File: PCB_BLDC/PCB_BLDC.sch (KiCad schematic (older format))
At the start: 61 parts, among them J10 Conn_01x06, J11 Conn_01x07, J12 Conn_01x06, J13 Conn_01x08, J16 Conn_01x08, J17 Conn_01x10, J8 VCC_Unregulated, J9 VCC_GND, Q1 IRF4905, SW1 Rotary_Encoder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

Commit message: Main: Finish PCB Routing Add Filled Zone Texts
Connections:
- net 5V is gone; now on net VCC_5V: A1.5 (+5V), J13.5 (Pin_5)
- net L1_Sense: now also J11.4 (Pin_4); no longer J11.3 (Pin_3)
- net L2_Sense: now also J11.3 (Pin_3); no longer J11.2 (Pin_2)
- net L3_Sense: now also J11.2 (Pin_2); no longer J11.1 (Pin_1)
- net VCC_5V: now also J11.1 (Pin_1); no longer A1.8 (VIN), J11.4 (Pin_4), J13.8 (Pin_8)
- new net VIN: A1.8 (VIN), J13.8 (Pin_8)
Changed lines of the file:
@@
 Wire Wire Line
 	4600 1150 4550 1150
-Text Label 3300 3500 0    50   ~ 0
+Text Label 3100 3500 2    50   ~ 0
 VCC_5V
 Wire Wire Line
@@
 VCC_Filtered
 Text Label 3100 2300 2    50   ~ 0
-VCC_Filtered
-Text Label 5950 1150 0    50   ~ 0
 VCC_Filtered
 Text Notes 1250 650  0    50   ~ 0
@@
 Wire Notes Line
 	3400 850  6450 850
-Wire Wire Line
-	3100 3450 3100 3500
 $Comp
 L power:GND #PWR01
@@
 Wire Wire Line
 	4700 1900 4700 2000
-Text Label 5500 5000 2    50   ~ 0
-VCC_5V
 Text Label 4900 6950 2    50   ~ 0
 Rot_A_Pull_Up
@@
 Wire Wire Line
 	850  1150 1400 1150
-Wire Wire Line
-	3300 3500 3100 3500
-Connection ~ 3100 3500
-Wire Wire Line
-	3100 3500 3100 3650
 Text Label 750  5450 2    50   ~ 0
 Reset
@@
 Wire Wire Line
 	1000 5550 750  5550
-Text Label 750  5650 2    50   ~ 0
-5V
 Wire Wire Line
 	750  5650 1000 5650
@@
 Text Label 6300 6050 0    50   ~ 0
 AREF
-Text Label 750  5950 2    50   ~ 0
+Text Label 750  5650 2    50   ~ 0
 VCC_5V
 Text Label 5700 5000 2    50   ~ 0
@@
 Wire Wire Line
 	5500 5000 5500 5250
-Text Label 5800 5000 0    50   ~ 0
-5V
 Text Label 5700 7450 0    50   ~ 0
 GND
@@
 Wire Wire Line
 	6300 6250 6100 6250
-Wire Wire Line
-	3100 2700 3100 2800
+$Comp
+L Connector_Generic:Conn_01x06 J10
+U 1 1 61CCE6B7
+P 750 7250
+F 0 "J10" H 830 7242 50  0000 L CNN
+F 1 "Conn_01x06" H 830 7151 50  0000 L CNN
+F 2 "Connector_PinSocket_2.54mm:PinSocket_1x06_P2.54mm_Vertical" H 750 7250 50  0001 C CNN
+F 3 "~" H 750 7250 50  0001 C CNN
+	1    750  7250
+	-1   0    0    -1
+$EndComp
+Wire Wire Line
+	1050 7550 950  7550
+Wire Wire Line
+	950  7450 1050 7450
+Wire Wire Line
+	950  7350 1050 7350
+Text Label 1050 7350 0    50   ~ 0
+L1_Sense
+Text Label 1050 7450 0    50   ~ 0
+L2_Sense
+Text Label 1050 7550 0    50   ~ 0
+L3_Sense
+$Comp
+L Connector_Generic:Conn_01x07 J11
+U 1 1 61E26882
+P 3200 7300
+F 0 "J11" H 3118 6775 50  0000 C CNN
+F 1 "Conn_01x07" H 3118 6866 50  0000 C CNN
+F 2 "TerminalBlock_Phoenix:TerminalBlock_Phoenix_MKDS-1,5-7_1x07_P5.00mm_Horizontal" H 3200 7300 50  0001 C CNN
+F 3 "~" H 3200 7300 50  0001 C CNN
+	1    3200 7300
+	-1   0    0    1
+$EndComp
+Text Label 3550 7500 0    50   ~ 0
+L3_Sense
+Text Label 3550 7400 0    50   ~ 0
+L2_Sense
+Text Label 3550 7300 0    50   ~ 0
+L1_Sense
+Text Label 3550 7200 0    50   ~ 0
+L3_Motor
+Text Label 3550 7100 0    50   ~ 0
+L2_Motor
+Text Label 3550 7600 0    50   ~ 0
+VCC_5V
+Wire Wire Line
+	3550 7000 3400 7000
+Wire Wire Line
+	3550 7100 3400 7100
+Wire Wire Line
+	3400 7200 3550 7200
+Wire Wire Line
+	3550 7300 3400 7300
+Wire Wire Line
+	3400 7400 3550 7400
+Wire Wire Line
+	3400 7600 3550 7600
+Wire Wire Line
+	3400 7500 3550 7500
+Text Label 3550 7000 0    50   ~ 0
+L1_Motor
+Text Label 5800 5000 0    50   ~ 0
+VCC_5V
+Text Label 5500 5000 2    50   ~ 0
+VIN
+Text Label 750  5950 2    50   ~ 0
+VIN
 $Comp
 L power:PWR_FLAG #FLG0103
 U 1 1 61C961E6
-P 5800 1150
-F 0 "#FLG0103" H 5800 1225 50  0001 C CNN
-F 1 "PWR_FLAG" H 5800 1323 50  0000 C CNN
-F 2 "" H 5800 1150 50  0001 C CNN
-F 3 "~" H 5800 1150 50  0001 C CNN
-	1    5800 1150
-	1    0    0    -1
-$EndComp
+P 5950 1150
+F 0 "#FLG0103" H 5950 1225 50  0001 C CNN
+F 1 "PWR_FLAG" H 5950 1323 50  0000 C CNN
+F 2 "" H 5950 1150 50  0001 C CNN
+F 3 "~" H 5950 1150 50  0001 C CNN
+	1    5950 1150
+	1    0    0    -1
+$EndComp
+Wire Wire Line
+	3100 2800 3100 2850
+Wire Wire Line
+	3100 2700 3100 2800
+Connection ~ 3100 2800
 $Comp
 L power:PWR_FLAG #FLG0104
@@
 	0    -1   -1   0
 $EndComp
-Connection ~ 3100 2800
-Wire Wire Line
-	3100 2800 3100 2850
-$Comp
-L Connector_Generic:Conn_01x06 J10
-U 1 1 61CCE6B7
-P 750 7250
-F 0 "J10" H 830 7242 50  0000 L CNN
-F 1 "Conn_01x06" H 830 7151 50  0000 L CNN
-F 2 "Connector_PinSocket_2.54mm:PinSocket_1x06_P2.54mm_Vertical" H 750 7250 50  0001 C CNN
-F 3 "~" H 750 7250 50  0001 C CNN
-	1    750  7250
-	-1   0    0    -1
-$EndComp
-Wire Wire Line
-	1050 7550 950  7550
-Wire Wire Line
-	950  7450 1050 7450
-Wire Wire Line
-	950  7350 1050 7350
-Text Label 1050 7350 0    50   ~ 0
-L1_Sense
-Text Label 1050 7450 0    50   ~ 0
-L2_Sense
-Text Label 1050 7550 0    50   ~ 0
-L3_Sense
-$Comp
-L Connector_Generic:Conn_01x07 J11
-U 1 1 61E26882
-P 3200 7300
-F 0 "J11" H 3118 6775 50  0000 C CNN
-F 1 "Conn_01x07" H 3118 6866 50  0000 C CNN
-F 2 "TerminalBlock_Phoenix:TerminalBlock_Phoenix_MKDS-1,5-7_1x07_P5.00mm_Horizontal" H 3200 7300 50  0001 C CNN
-F 3 "~" H 3200 7300 50  0001 C CNN
-	1    3200 7300
-	-1   0    0    1
-$EndComp
-Text Label 3550 7600 0    50   ~ 0
-L3_Sense
-Text Label 3550 7500 0    50   ~ 0
-L2_Sense
-Text Label 3550 7400 0    50   ~ 0
-L1_Sense
-Text Label 3550 7200 0    50   ~ 0
-L3_Motor
-Text Label 3550 7100 0    50   ~ 0
-L2_Motor
-Text Label 3550 7300 0    50   ~ 0
-VCC_5V
-Wire Wire Line
-	3550 7000 3400 7000
-Wire Wire Line
-	3550 7100 3400 7100
-Wire Wire Line
-	3400 7200 3550 7200
-Wire Wire Line
-	3550 7300 3400 7300
-Wire Wire Line
-	3400 7400 3550 7400
-Wire Wire Line
-	3400 7600 3550 7600
-Wire Wire Line
-	3400 7500 3550 7500
-Text Label 3550 7000 0    50   ~ 0
-L1_Motor
+Wire Wire Line
+	3100 3450 3100 3650
+Text Label 5550 1150 1    50   ~ 0
+VCC_Filtered
 $EndSCHEMATC

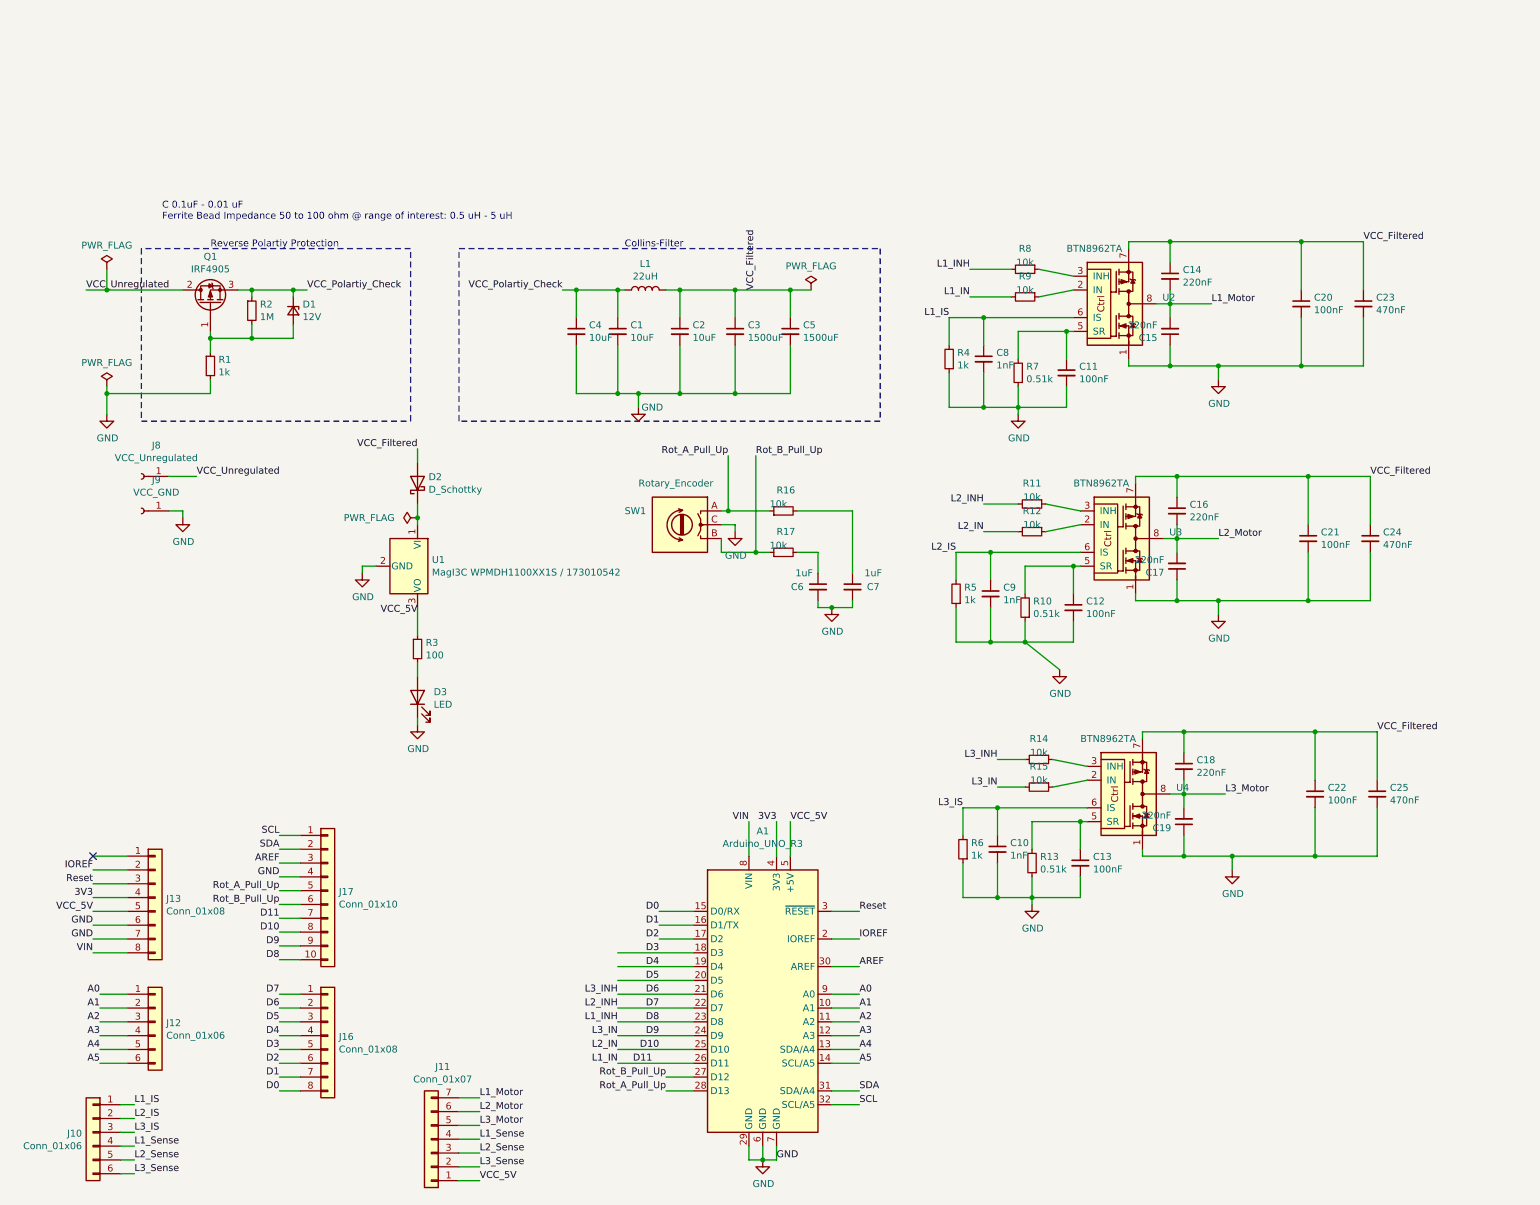
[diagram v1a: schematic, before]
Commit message: Main: Add Text to Schematic and PCB, Images
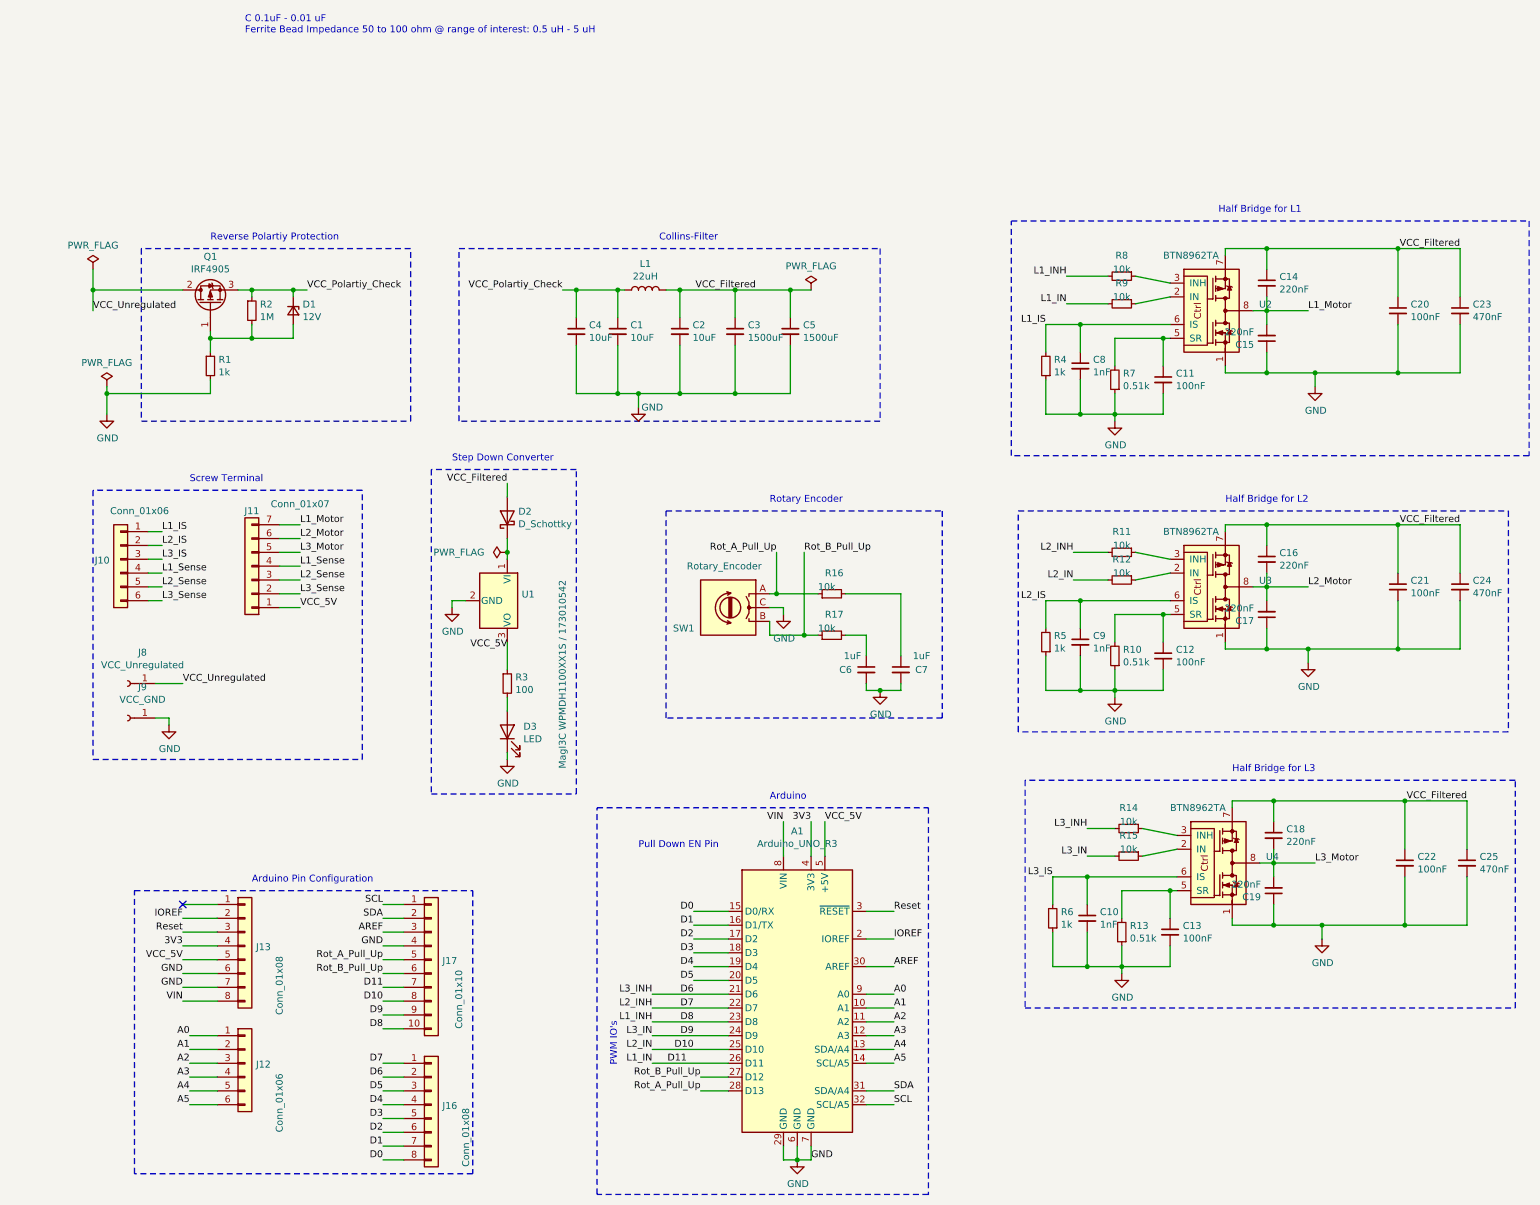
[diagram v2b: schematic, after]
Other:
- note added: "Arduino Pin Configuration\n"
- note added: "Arduino\n"
- note added: "Half Bridge for L1"
- note added: "Half Bridge for L2\n"
- note added: "Half Bridge for L3\n"
- note added: "PWM IO's"
- note added: "Pull Down EN Pin\n"
- note added: "Rotary Encoder"
- note added: "Screw Terminal"
- note added: "Step Down Converter\n"
- moved on the sheet: A1, C10, C11, C12, C13, C14, C15, C16, C17, C18, C19, C20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

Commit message: Main: Update PCB, Add Vias, Update Schematic, Update Netlist
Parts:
- removed J11: Conn_01x07, TerminalBlock_Phoenix:TerminalBlock_Phoenix_MKDS-1,5-7_1x07_P5.00mm_Horizontal, symbol Connector_Generic:Conn_01x07
- removed J9: VCC_GND, Connector:Banana_Jack_1Pin, symbol Connector:Conn_01x01_Female
- added J1: Conn_01x08, TerminalBlock_Phoenix:TerminalBlock_Phoenix_MKDS-1,5-8_1x08_P5.00mm_Horizontal, symbol Connector_Generic:Conn_01x08
- C1, C2, C4: footprint Capacitor_SMD:C_1206_3216Metric_Pad1.33x1.80mm_HandSolder -> Capacitor_SMD:C_1210_3225Metric_Pad1.33x2.70mm_HandSolder
- J8: value VCC_Unregulated -> Power Terminal; footprint Connector:Banana_Jack_1Pin -> Connector:Banana_Jack_2Pin; symbol Connector:Conn_01x01_Female -> Connector:Conn_01x02_Female
- R3: value 100 -> 150
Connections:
- net GND: now also J8.2 (Pin_2), J1.1 (Pin_1)
- net L1_Motor: now also J1.8 (Pin_8)
- net L1_Sense: now also J1.5 (Pin_5)
- net L2_Motor: now also J1.7 (Pin_7)
- net L2_Sense: now also J1.4 (Pin_4)
- net L3_Motor: now also J1.6 (Pin_6)
- net L3_Sense: now also J1.3 (Pin_3)
- net VCC_5V: now also J1.2 (Pin_2)
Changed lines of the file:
@@
 F 0 "C1" H 4642 1496 50  0000 L CNN
 F 1 "10uF" H 4642 1405 50  0000 L CNN
-F 2 "Capacitor_SMD:C_1206_3216Metric_Pad1.33x1.80mm_HandSolder" H 4550 1450 50  0001 C CNN
+F 2 "Capacitor_SMD:C_1210_3225Metric_Pad1.33x2.70mm_HandSolder" H 4550 1450 50  0001 C CNN
 F 3 "~" H 4550 1450 50  0001 C CNN
 	1    4550 1450
@@
 P 3750 4000
 F 0 "R3" H 3809 4046 50  0000 L CNN
-F 1 "100" H 3809 3955 50  0000 L CNN
+F 1 "150" H 3809 3955 50  0000 L CNN
 F 2 "Resistor_SMD:R_1206_3216Metric_Pad1.30x1.75mm_HandSolder" H 3750 4000 50  0001 C CNN
 F 3 "~" H 3750 4000 50  0001 C CNN
@@
 F 0 "C2" H 5092 1496 50  0000 L CNN
 F 1 "10uF" H 5092 1405 50  0000 L CNN
-F 2 "Capacitor_SMD:C_1206_3216Metric_Pad1.33x1.80mm_HandSolder" H 5000 1450 50  0001 C CNN
+F 2 "Capacitor_SMD:C_1210_3225Metric_Pad1.33x2.70mm_HandSolder" H 5000 1450 50  0001 C CNN
 F 3 "~" H 5000 1450 50  0001 C CNN
 	1    5000 1450
@@
 F 0 "C4" H 4342 1496 50  0000 L CNN
 F 1 "10uF" H 4342 1405 50  0000 L CNN
-F 2 "Capacitor_SMD:C_1206_3216Metric_Pad1.33x1.80mm_HandSolder" H 4250 1450 50  0001 C CNN
+F 2 "Capacitor_SMD:C_1210_3225Metric_Pad1.33x2.70mm_HandSolder" H 4250 1450 50  0001 C CNN
 F 3 "~" H 4250 1450 50  0001 C CNN
 	1    4250 1450
@@
 Connection ~ 5400 1150
 $Comp
-L Connector:Conn_01x01_Female J8
-U 1 1 6185108B
-P 1000 4000
-F 0 "J8" H 892 3775 50  0000 C CNN
-F 1 "VCC_Unregulated" H 892 3866 50  0000 C CNN
-F 2 "Connector:Banana_Jack_1Pin" H 1000 4000 50  0001 C CNN
-F 3 "~" H 1000 4000 50  0001 C CNN
-	1    1000 4000
-	-1   0    0    1
-$EndComp
-$Comp
-L Connector:Conn_01x01_Female J9
-U 1 1 6185195D
-P 1000 4250
-F 0 "J9" H 892 4025 50  0000 C CNN
-F 1 "VCC_GND" H 892 4116 50  0000 C CNN
-F 2 "Connector:Banana_Jack_1Pin" H 1000 4250 50  0001 C CNN
-F 3 "~" H 1000 4250 50  0001 C CNN
-	1    1000 4250
-	-1   0    0    1
-$EndComp
-$Comp
 L power:GND #PWR03
 U 1 1 6185A87A
-P 1300 4300
-F 0 "#PWR03" H 1300 4050 50  0001 C CNN
-F 1 "GND" H 1305 4127 50  0000 C CNN
-F 2 "" H 1300 4300 50  0001 C CNN
-F 3 "" H 1300 4300 50  0001 C CNN
-	1    1300 4300
-	1    0    0    -1
-$EndComp
-Wire Wire Line
-	1200 4250 1300 4250
-Wire Wire Line
-	1300 4250 1300 4300
+P 1500 4100
+F 0 "#PWR03" H 1500 3850 50  0001 C CNN
+F 1 "GND" H 1505 3927 50  0000 C CNN
+F 2 "" H 1500 4100 50  0001 C CNN
+F 3 "" H 1500 4100 50  0001 C CNN
+	1    1500 4100
+	1    0    0    -1
+$EndComp
+Wire Wire Line
+	1500 4050 1500 4100
 $Comp
 L power:GND #PWR0108
@@
 Wire Wire Line
 	7950 5250 8150 5250
-Text Label 1400 4000 0    50   ~ 0
+Text Label 1400 3950 2    50   ~ 0
 VCC_Unregulated
 Wire Wire Line
-	1200 4000 1400 4000
+	1600 3950 1400 3950
 Text Label 750  1300 0    50   ~ 0
 VCC_Unregulated
@@
 Text Label 2250 3350 0    50   ~ 0
 L3_Sense
-$Comp
-L Connector_Generic:Conn_01x07 J11
-U 1 1 61E26882
-P 1900 3150
-F 0 "J11" H 1900 2750 50  0000 C CNN
-F 1 "Conn_01x07" H 1550 2700 50  0000 C CNN
-F 2 "TerminalBlock_Phoenix:TerminalBlock_Phoenix_MKDS-1,5-7_1x07_P5.00mm_Horizontal" H 1900 3150 50  0001 C CNN
-F 3 "~" H 1900 3150 50  0001 C CNN
-	1    1900 3150
-	-1   0    0    1
-$EndComp
 Wire Wire Line
 	750  1300 750  1150
@@
 	3500 7550 1050 7550
 Wire Notes Line
-	1050 7550 1050 5500
-Wire Notes Line
 	750  4550 2700 4550
-Wire Notes Line
-	2700 4550 2700 2600
 Wire Notes Line
 	2700 2600 750  2600
@@
 Text Notes 9000 4650 0    50   ~ 0
 Half Bridge for L3\n
+$Comp
+L Connector_Generic:Conn_01x08 J1
+U 1 1 6188649B
+P 1900 3250
+F 0 "J1" H 1980 3242 50  0000 L CNN
+F 1 "Conn_01x08" V 2150 2750 50  0000 L CNN
+F 2 "TerminalBlock_Phoenix:TerminalBlock_Phoenix_MKDS-1,5-8_1x08_P5.00mm_Horizontal" H 1900 3250 50  0001 C CNN
+F 3 "~" H 1900 3250 50  0001 C CNN
+	1    1900 3250
+	-1   0    0    1
+$EndComp
+$Comp
+L power:GND #PWR0103
+U 1 1 6188811D
+P 2200 3600
+F 0 "#PWR0103" H 2200 3350 50  0001 C CNN
+F 1 "GND" H 2205 3427 50  0000 C CNN
+F 2 "" H 2200 3600 50  0001 C CNN
+F 3 "" H 2200 3600 50  0001 C CNN
+	1    2200 3600
+	1    0    0    -1
+$EndComp
+Wire Wire Line
+	2100 3550 2200 3550
+Wire Wire Line
+	2200 3550 2200 3600
+$Comp
+L Connector:Conn_01x02_Female J8
+U 1 1 6185108B
+P 1800 3950
+F 0 "J8" H 1692 3725 50  0000 C CNN
+F 1 "Power Terminal" H 1550 4100 50  0000 C CNN
+F 2 "Connector:Banana_Jack_2Pin" H 1800 3950 50  0001 C CNN
+F 3 "~" H 1800 3950 50  0001 C CNN
+	1    1800 3950
+	1    0    0    -1
+$EndComp
+Wire Wire Line
+	1500 4050 1600 4050
+Wire Notes Line
+	1050 5500 1050 7550
+Wire Notes Line
+	2700 2600 2700 4550
 $EndSCHEMATC

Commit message: Main: Update Schematic, Add Vias, RC-Filt for Hall-Sense
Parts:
- removed J1: Conn_01x08, TerminalBlock_Phoenix:TerminalBlock_Phoenix_MKDS-1,5-8_1x08_P5.00mm_Horizontal, symbol Connector_Generic:Conn_01x08
- removed J10: Conn_01x06, Connector_PinSocket_2.54mm:PinSocket_1x06_P2.54mm_Vertical, symbol Connector_Generic:Conn_01x06
- added J1: Power Terminal, Connector:Banana_Jack_1Pin, symbol Connector_Generic:Conn_01x01
- added J2: Conn_01x03, TerminalBlock_Phoenix:TerminalBlock_Phoenix_MKDS-1,5-3_1x03_P5.00mm_Horizontal, symbol Connector_Generic:Conn_01x03
- added J3: Conn_01x05, TerminalBlock_Phoenix:TerminalBlock_Phoenix_MKDS-1,5-5_1x05_P5.00mm_Horizontal, symbol Connector_Generic:Conn_01x05
- J8: footprint Connector:Banana_Jack_2Pin -> Connector:Banana_Jack_1Pin; symbol Connector:Conn_01x02_Female -> Connector_Generic:Conn_01x01
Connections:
- net L1_IS is gone; now on net A0: C8.1, R4.2, U2.6 (IS)
- net L2_IS is gone; now on net A1: C9.1, R5.2, U3.6 (IS)
- net L3_IS is gone; now on net A2: C10.1, R6.2, U4.6 (IS)
- net D2: now also J3.3 (Pin_3)
- net D3: now also J3.4 (Pin_4)
- net D4: now also J3.5 (Pin_5)
- net GND: now also J1.1 (Pin_1), J3.1 (Pin_1); no longer J8.2 (Pin_2)
- net L1_Motor: now also J2.3 (Pin_3)
- net L2_Motor: now also J2.2 (Pin_2)
- net L3_Motor: now also J2.1 (Pin_1)
- net VCC_5V: now also J3.2 (Pin_2)
- net Rot_A_Pull_Up renamed D13
- net Rot_B_Pull_Up renamed D12
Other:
- moved on the sheet: J12, J13
